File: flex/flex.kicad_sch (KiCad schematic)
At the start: 93 parts, among them J1 Conn_01x06_Female, J2 Conn_01x05_Female, J3 Conn_01x03_Female, J4 Conn_01x06_Female, J5 Conn_01x03_Female, SW1 SW_Push, SW10 SW_Push, SW11 SW_Push, SW12 SW_Push, SW14 SW_Push, SW15 SW_Push, SW16 SW_Push, SW17 SW_Push, SW19 SW_Push, SW2 SW_Push, SW20 SW_Push, SW21 SW_Push, SW22 SW_Push, SW23 SW_Push, SW24 SW_Push, SW25 SW_Push, SW26 SW_Push, SW3 SW_Push, SW4 SW_Push, SW5 SW_Push, SW6 SW_Push, SW7 SW_Push, SW8 SW_Push, SW9 SW_Push

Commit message: added hotswap footprint
currently incomplete, imported daprice's Kailh footprint and modified it to fit flip it horizontally.
Will continue some other time.
Major kudos to bastardkb for already making the pcb flippable!
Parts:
- SW1, SW10, SW11, SW12, SW14, SW15, SW16, SW17, SW19, SW2, SW20, SW21, SW22, SW23, SW24, SW25, SW26, SW3, SW4, SW5, SW6, SW7, SW8, SW9: footprint custom:SW_MX_reversible -> Kailh_sockets:Kailh_socket_MX_flippable

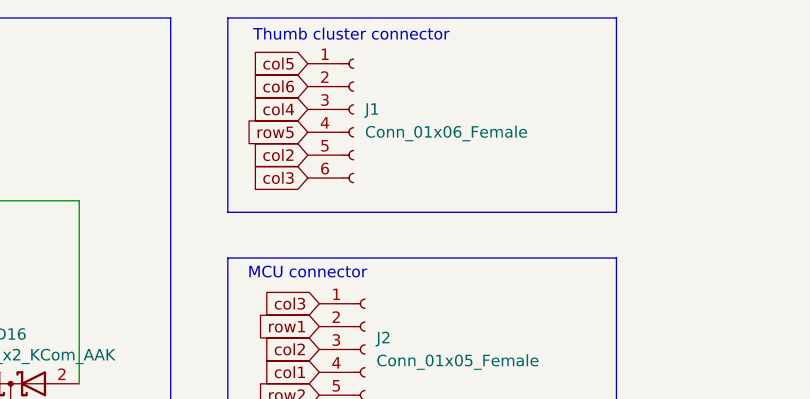
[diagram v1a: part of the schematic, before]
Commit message: Routed diodes
now only the planes need to connect
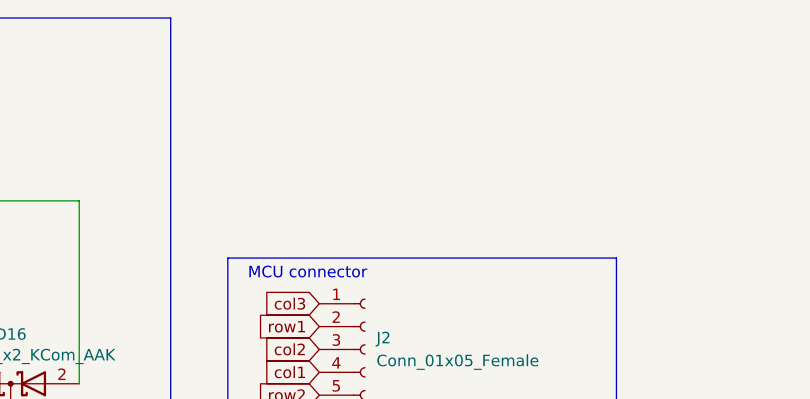
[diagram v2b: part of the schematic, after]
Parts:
- removed J1: Conn_01x06_Female, Connector_PinHeader_2.54mm:PinHeader_1x06_P2.54mm_Vertical, symbol Connector:Conn_01x06_Female
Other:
- note removed: "Thumb cluster connector"
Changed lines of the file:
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@@
     (stroke (width 0) (type solid) (color 0 0 0 0))
   )
-  (polyline (pts (xy 350.52 19.05) (xy 393.7 19.05))
-    (stroke (width 0) (type default) (color 0 0 0 0))
-  )
   (wire (pts (xy 38.1 72.39) (xy 38.1 76.2))
     (stroke (width 0) (type solid) (color 0 0 0 0))
@@
     (stroke (width 0) (type solid) (color 0 0 0 0))
   )
-  (polyline (pts (xy 393.7 40.64) (xy 350.52 40.64))
-    (stroke (width 0) (type default) (color 0 0 0 0))
-  )
   (wire (pts (xy 300.99 148.59) (xy 304.8 148.59))
     (stroke (width 0) (type solid) (color 0 0 0 0))
@@
     (stroke (width 0) (type solid) (color 0 0 0 0))
   )
-  (polyline (pts (xy 393.7 19.05) (xy 393.7 40.64))
-    (stroke (width 0) (type default) (color 0 0 0 0))
-  )
   (wire (pts (xy 193.04 187.96) (xy 215.9 187.96))
     (stroke (width 0) (type solid) (color 0 0 0 0))
@@
     (stroke (width 0) (type solid) (color 0 0 0 0))
   )
-  (polyline (pts (xy 350.52 19.05) (xy 350.52 40.64))
-    (stroke (width 0) (type default) (color 0 0 0 0))
-  )
   (wire (pts (xy 198.12 50.8) (xy 250.19 50.8))
     (stroke (width 0) (type solid) (color 0 0 0 0))
@@
     (effects (font (size 1.27 1.27)) (justify right bottom))
   )
-  (text "Thumb cluster connector" (at 375.158 21.844 180)
-    (effects (font (size 1.27 1.27)) (justify right bottom))
-  )
   (text "This work is licensed under a Creative Commons Attribution-NonCommercial-ShareAlike 4.0 International License."
     (at 429.26 378.46 0)
@@
     )
   )
-  (global_label "col2" (shape input) (at 359.41 34.29 180)
-    (effects (font (size 1.27 1.27)) (justify right))
-    (property "Intersheet References" "${INTERSHEET_REFS}" (id 0) (at 334.01 1.905 0)
-      (effects (font (size 1.27 1.27)) hide)
-    )
-  )
   (global_label "Din" (shape input) (at 374.65 101.6 180)
     (effects (font (size 1.27 1.27)) (justify right))
@@
     )
   )
-  (global_label "row5" (shape input) (at 359.41 31.75 180)
-    (effects (font (size 1.27 1.27)) (justify right))
-    (property "Intersheet References" "${INTERSHEET_REFS}" (id 0) (at 334.01 1.905 0)
-      (effects (font (size 1.27 1.27)) hide)
-    )
-  )
   (global_label "col2" (shape input) (at 360.68 55.88 180)
     (effects (font (size 1.27 1.27)) (justify right))
@@
     )
   )
-  (global_label "col4" (shape input) (at 359.41 29.21 180)
-    (effects (font (size 1.27 1.27)) (justify right))
-    (property "Intersheet References" "${INTERSHEET_REFS}" (id 0) (at 334.01 1.905 0)
-      (effects (font (size 1.27 1.27)) hide)
-    )
-  )
-  (global_label "col3" (shape input) (at 359.41 36.83 180)
-    (effects (font (size 1.27 1.27)) (justify right))
-    (property "Intersheet References" "${INTERSHEET_REFS}" (id 0) (at 334.01 1.905 0)
-      (effects (font (size 1.27 1.27)) hide)
-    )
-  )
   (global_label "col4" (shape input) (at 185.42 30.48 90)
     (effects (font (size 1.27 1.27)) (justify left))
@@
     )
   )
-  (global_label "col6" (shape input) (at 359.41 26.67 180)
-    (effects (font (size 1.27 1.27)) (justify right))
-    (property "Intersheet References" "${INTERSHEET_REFS}" (id 0) (at 334.01 1.905 0)
-      (effects (font (size 1.27 1.27)) hide)
-    )
-  )
   (global_label "col6" (shape input) (at 294.64 29.21 90)
     (effects (font (size 1.27 1.27)) (justify left))
@@
     )
   )
-  (global_label "col5" (shape input) (at 359.41 24.13 180)
-    (effects (font (size 1.27 1.27)) (justify right))
-    (property "Intersheet References" "${INTERSHEET_REFS}" (id 0) (at 334.01 1.905 0)
-      (effects (font (size 1.27 1.27)) hide)
-    )
-  )
   (global_label "col2" (shape input) (at 81.28 30.48 90)
     (effects (font (size 1.27 1.27)) (justify left))
@@
     (pin "4")
   )
-  (symbol (lib_id "Connector:Conn_01x06_Female") (at 364.49 29.21 0) (unit 1)
-    (in_bom yes) (on_board yes)
-    (property "Reference" "J1" (id 0) (at 365.76 29.21 0)
-      (effects (font (size 1.27 1.27)) (justify left))
-    )
-    (property "Value" "Conn_01x06_Female" (id 1) (at 365.76 31.75 0)
-      (effects (font (size 1.27 1.27)) (justify left))
-    )
-    (property "Footprint" "Connector_PinHeader_2.54mm:PinHeader_1x06_P2.54mm_Vertical" (id 2) (at 364.49 29.21 0)
-      (effects (font (size 1.27 1.27)) hide)
-    )
-    (property "Datasheet" "~" (id 3) (at 364.49 29.21 0)
-      (effects (font (size 1.27 1.27)) hide)
-    )
-    (pin "1")
-    (pin "2")
-    (pin "3")
-    (pin "4")
-    (pin "5")
-    (pin "6")
-  )
   (symbol (lib_id "LED:SK6812MINI") (at 281.94 173.99 0) (unit 1)
     (in_bom yes) (on_board yes)
@@
       (reference "D60") (unit 1) (value "SK6812MINI") (footprint "libs2:YS-SK6812MINI-E_REVERSE_NO_EDGECUT")
     )
-    (path "/ee78fe8c-fb5c-4fdf-aa0b-177539f4ed2a"
-      (reference "J1") (unit 1) (value "Conn_01x06_Female") (footprint "Connector_PinHeader_2.54mm:PinHeader_1x06_P2.54mm_Vertical")
-    )
     (path "/a43a3629-0581-4a28-b6ed-b6a23369a385"
